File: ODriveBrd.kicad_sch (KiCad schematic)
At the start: 5 parts, among them J1 ODrive, J2 CAN, J3 UART, J4 ENC A, J5 ENC B

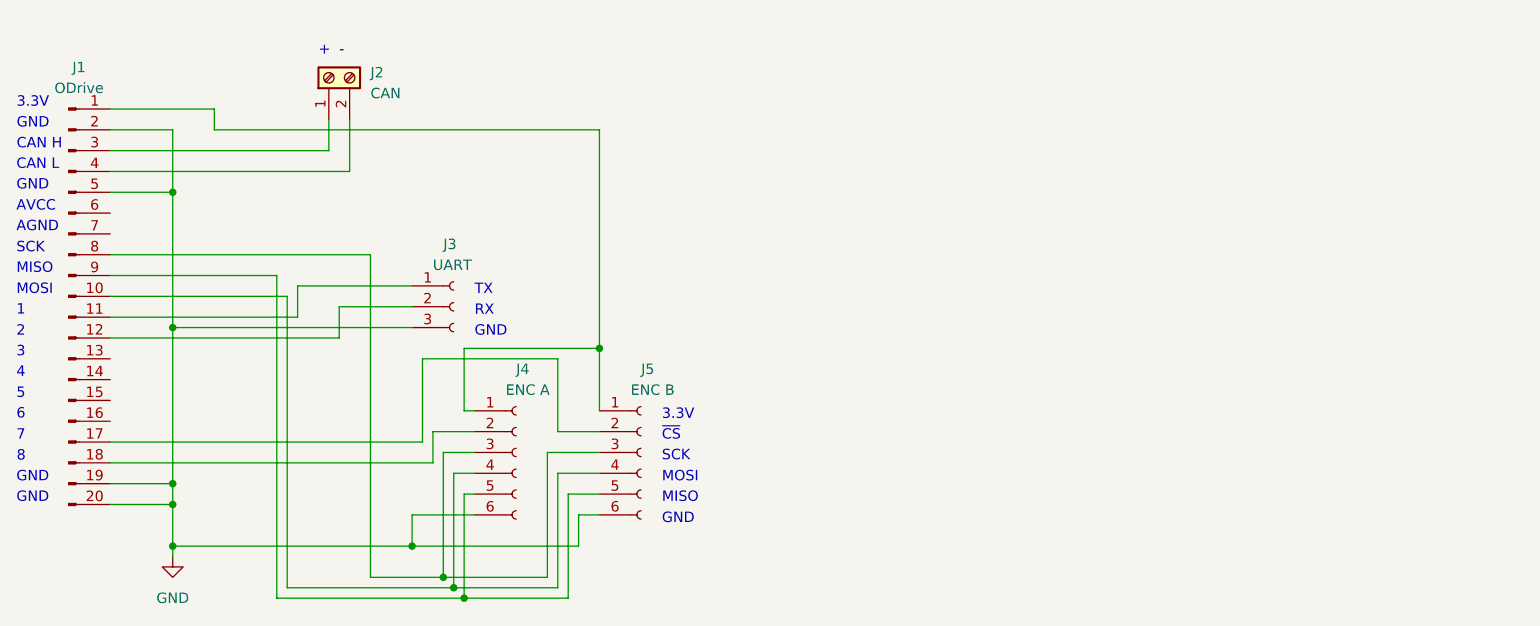
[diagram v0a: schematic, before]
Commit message: Updated ODrive adapter with isolated serial.
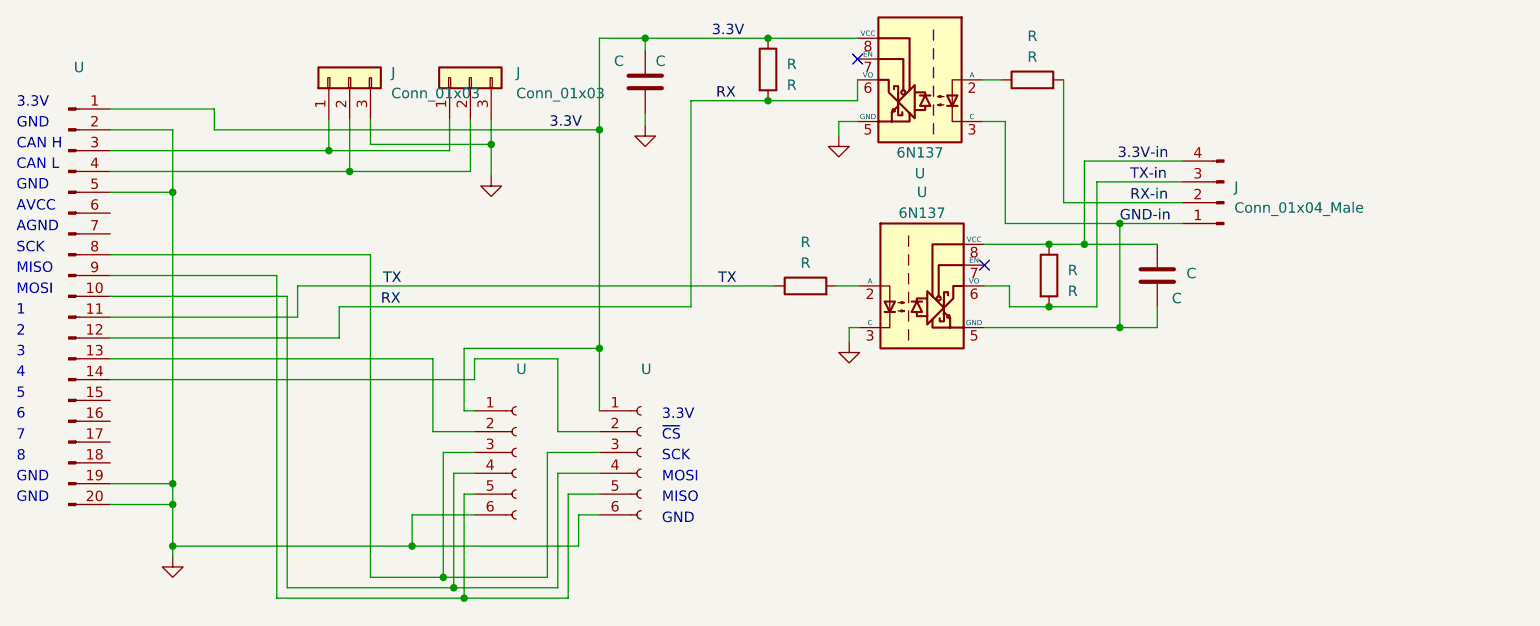
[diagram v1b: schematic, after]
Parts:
- removed J2: CAN, TerminalBlock_MetzConnect:TerminalBlock_MetzConnect_Type059_RT06302HBWC_1x02_P3.50mm_Horizontal, symbol Connector:Screw_Terminal_01x02
- removed J3: UART, Connector_PinSocket_2.54mm:PinSocket_1x03_P2.54mm_Horizontal, symbol Connector:Conn_01x03_Female
- added C (x2): C, symbol Device:C
- added J: Conn_01x04_Male, symbol Connector:Conn_01x04_Male
- added J (x2): Conn_01x03, symbol Connector_Generic:Conn_01x03
- added R (x4): R, symbol Device:R
- added U (x2): 6N137, Package_DIP:DIP-8_W7.62mm, symbol Isolator:6N137
- U: renamed from J5; value ENC B -> (none); footprint Connector_PinSocket_2.54mm:PinSocket_1x06_P2.54mm_Horizontal -> (none); JLC Part # (none) -> C8876
- U: renamed from J1; value ODrive -> (none); footprint Connector_PinHeader_2.54mm:PinHeader_1x20_P2.54mm_Vertical -> (none)
- U: renamed from J4; value ENC A -> (none); footprint Connector_PinSocket_2.54mm:PinSocket_1x06_P2.54mm_Horizontal -> (none); JLC Part # (none) -> C8876
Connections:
- net GND: now also C.2, J.3 (Pin_3), J.3 (Pin_3), U.3 (C), U.5 (GND)
- net 3.3V: now reaches U.1 (Pin_1), U.1 (Pin_1), U.1 (Pin_1)
- net 3.3V: now also C.1, R.1, U.8 (VCC)
- net at U.2 (Pin_2): now also U.14 (Pin_14); no longer U.17 (Pin_17)
- net at U.3 (Pin_3): now also J.1 (Pin_1), J.1 (Pin_1)
- net at U.4 (Pin_4): now also J.2 (Pin_2), J.2 (Pin_2)
- net TX: now reaches U.11 (Pin_11)
- net TX: now also R.1
- net RX: now reaches U.12 (Pin_12)
- net RX: now also R.2, U.6 (VO)
- net at U.13 (Pin_13): now also U.2 (Pin_2)
- net at U.18 (Pin_18): no longer U.2 (Pin_2)
- new net: R.1, U.2 (A)
- new net: R.2, U.2 (A)
- new net 3.3V-in: C.1, J.4 (Pin_4), R.1, U.8 (VCC)
- new net GND-in: C.2, J.1 (Pin_1), U.3 (C), U.5 (GND)
- new net RX-in: J.2 (Pin_2), R.2
- new net TX-in: J.3 (Pin_3), R.2, U.6 (VO)
- no-connect marks 0 -> 2
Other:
- note removed: "+"
- note removed: "-"
- note removed: "RX"
- note removed: "TX"

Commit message: Add inverters to the opto serial adapter.
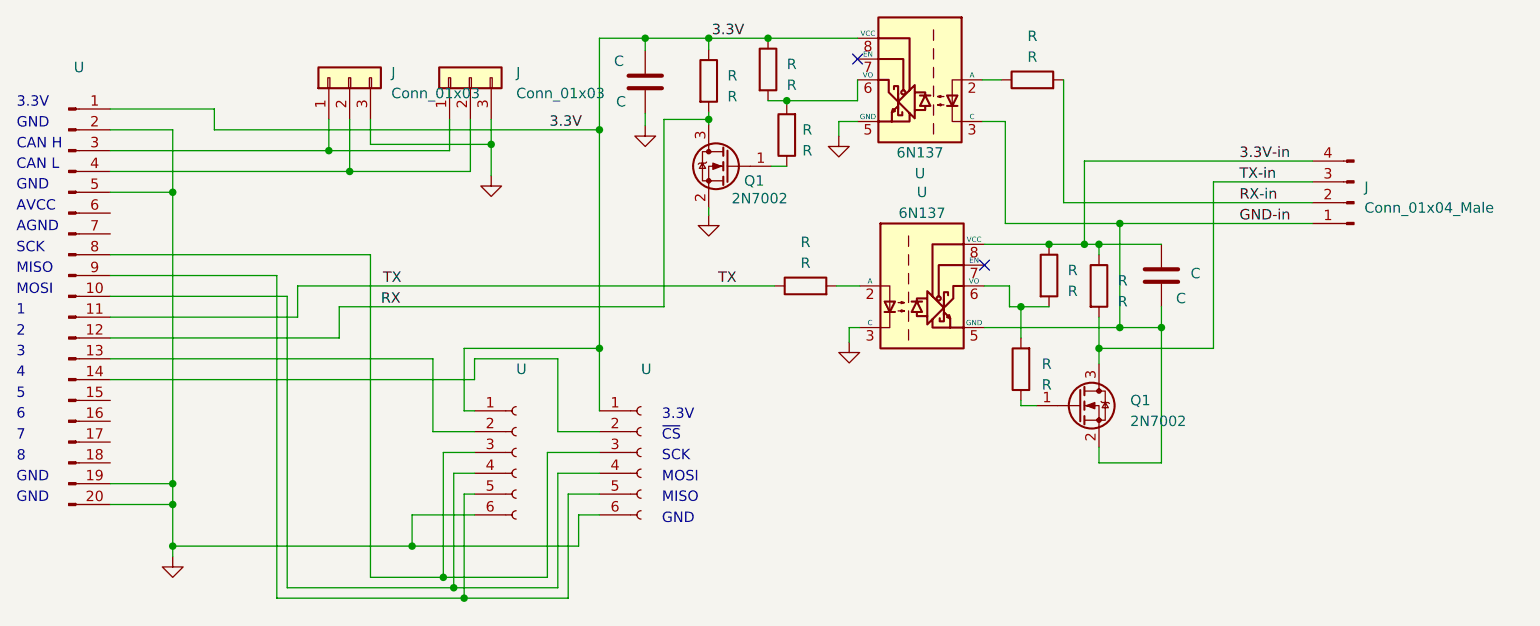
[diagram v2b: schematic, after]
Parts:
- added Q1 (x2): 2N7002, Package_TO_SOT_SMD:SOT-23, symbol Transistor_FET:2N7002
- added R (x4): R, symbol Device:R
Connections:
- net 3.3V: now also R.1
- net 3.3V-in: now also R.1
- net GND: now also Q1.2 (S)
- net GND-in: now also Q1.2 (S)
- net RX: now also Q1.3 (D), R.2; no longer R.2, U.6 (VO)
- net TX-in: now also Q1.3 (D), R.2; no longer R.2, U.6 (VO)
- new net: R.2, R.2, U.6 (VO) (x2)
- new net: Q1.1 (G), R.1 (x2)
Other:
- moved on the sheet: C, J
